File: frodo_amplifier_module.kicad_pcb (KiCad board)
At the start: 4 copper layers, 22.5 x 15 mm, 42 parts, among them IC1 INA826AID, J1 JST-GH, J2 JST-GH, J3 Conn_01x02_Socket, J5 Conn_01x04_Socket, U2 MCP6001-OT, U3 MIC5504-3.3YM5, U4 ADC101C021CIMM

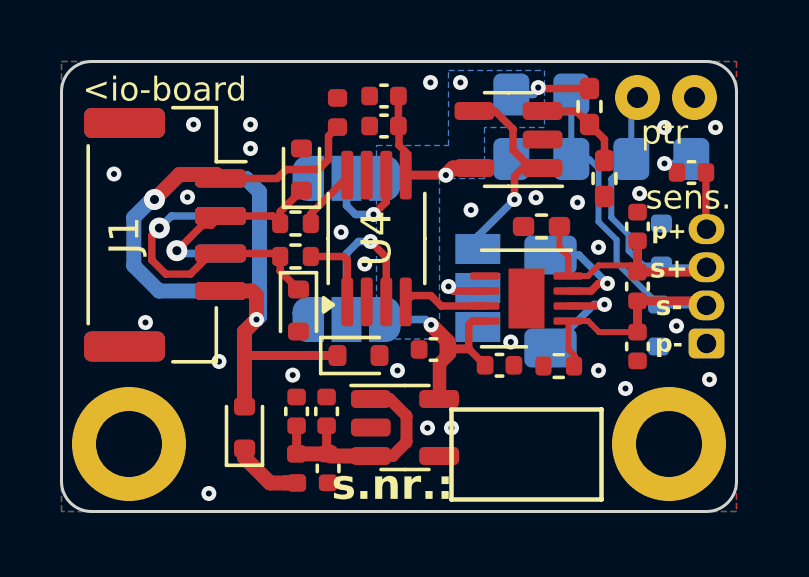
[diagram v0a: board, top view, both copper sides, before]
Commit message: added lcsc numbers
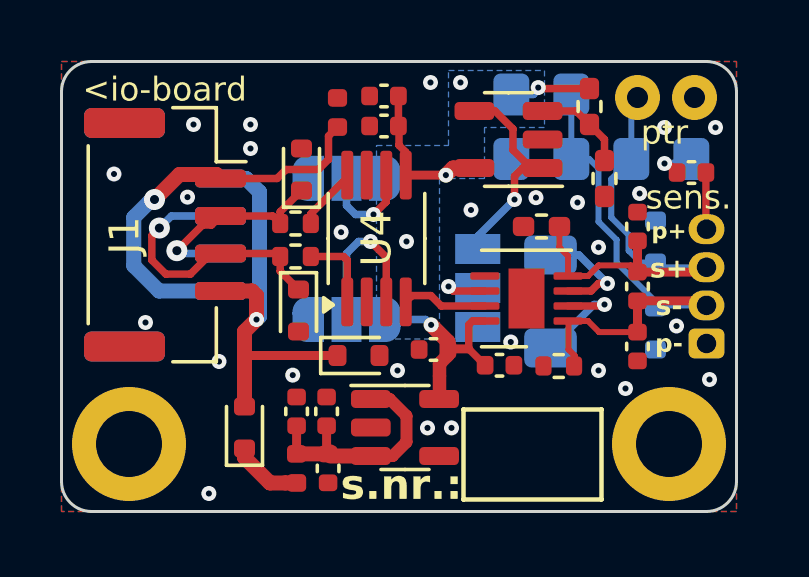
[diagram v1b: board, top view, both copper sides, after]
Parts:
- D1: value 1N4148WT -> 1SS424
- D2, D3, D7, D8: value ESD5Zxx -> ESD5Z36
- moved D3 2.81 mm to (70.3, 42.9), turned to -90 degrees
- moved D2 2.80 mm to (70.3, 40.0), turned to 90 degrees
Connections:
- D2 pad 1: s- -> s+
- D3 pad 1: s+ -> s-
